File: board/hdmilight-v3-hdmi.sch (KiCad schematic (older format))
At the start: 41 parts, among them J2 HDMI_A, Q2 BSS123, Q3 BSS123, Q4 BSS123, U4 ADV7611, U6 TPD12S520, Y2 28.63636MHz

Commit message: Fixed bugs in v3.0 board:
 * Changed FPGA GPIO to 2 row with ground to make it compatible with logic analyser plug for debugging
 * Move position sensor from PB4 to PB5
 * Connect voltage regulator center pad to ground pins
 * Add SPI CS line between FPGA and MCU
 * Move HDMI hotplug LED back from board edge
 * Move HDMI ESD chip closer to connector
 * Swap serial rx/tx
 * Fix FPGA EEPROM footprint
 * Fix reset button footprint
 * Connect ADV I2C to MCU
 * Fix missing ground to hotplug power off circuit
 * Move LED power connector to back of board
 * Move standby button to front of board
 * Only use HDMI 5v for hotplug detect
 * Change LED power switching to high side to stop it grounding back through the data line
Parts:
- R60: value 1K -> 2K2
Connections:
- net GND: now also Q2.2 (S), Q4.2 (S)
- net HDMI_5V: no longer C10.1, R14.1, R15.1, R60.2, U6.1 (5V)
- new net +5V: C10.1, R14.1, R15.1, R60.2, U6.1 (5V)
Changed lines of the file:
@@
 Wire Wire Line
 	2400 1300 2400 950
-Wire Wire Line
-	2400 950  2450 950
 Connection ~ 2400 1300
 Wire Wire Line
 	2400 1300 2550 1300
-Text GLabel 2450 950  2    50   Input ~ 0
-HDMI_5V
-Wire Wire Line
-	3800 1250 3900 1250
 Wire Wire Line
 	3800 1250 3800 1400
-Text GLabel 3900 1250 2    50   Input ~ 0
-HDMI_5V
 $Comp
 L Transistor_FET:BSS123 Q3
@@
 P 5850 4050
 F 0 "R60" V 6057 4050 50  0000 C CNN
-F 1 "1K" V 5966 4050 50  0000 C CNN
+F 1 "2K2" V 5966 4050 50  0000 C CNN
 F 2 "Resistor_SMD:R_0603_1608Metric" V 5780 4050 50  0001 C CNN
 F 3 "~" H 5850 4050 50  0001 C CNN
@@
 $EndComp
 Wire Wire Line
-	6000 4050 6100 4050
+	6000 4050 6200 4050
 Wire Wire Line
 	5600 4050 5700 4050
@@
 	2200 5750 2200 5450
 Wire Wire Line
-	1850 5750 2200 5750
+	1850 5750 2050 5750
 Wire Wire Line
 	1850 5700 1850 5750
@@
 	600  4700 2800 4700
 Wire Notes Line
-	2800 4700 2800 6000
-Wire Notes Line
-	2800 6000 600  6000
-Wire Notes Line
-	600  6000 600  4700
-Text Notes 1850 5950 2    50   ~ 0
+	2800 4700 2800 6050
+Wire Notes Line
+	2800 6050 600  6050
+Wire Notes Line
+	600  6050 600  4700
+Text Notes 1850 6000 2    50   ~ 0
 Pull HPD low when powered off
 $Comp
@@
 	1    0    0    -1
 $EndComp
-Text GLabel 6100 4050 2    50   Input ~ 0
-HDMI_5V
 $Comp
 L Device:Crystal_Small Y2
@@
 	1000 4100 1100 4100
 NoConn ~ 1700 3500
+$Comp
+L power:+5V #PWR0194
+U 1 1 5E441643
+P 2400 950
+F 0 "#PWR0194" H 2400 800 50  0001 C CNN
+F 1 "+5V" H 2415 1123 50  0000 C CNN
+F 2 "" H 2400 950 50  0001 C CNN
+F 3 "" H 2400 950 50  0001 C CNN
+	1    2400 950
+	1    0    0    -1
+$EndComp
+$Comp
+L power:+5V #PWR0195
+U 1 1 5E44BA2A
+P 3800 1250
+F 0 "#PWR0195" H 3800 1100 50  0001 C CNN
+F 1 "+5V" H 3815 1423 50  0000 C CNN
+F 2 "" H 3800 1250 50  0001 C CNN
+F 3 "" H 3800 1250 50  0001 C CNN
+	1    3800 1250
+	1    0    0    -1
+$EndComp
+$Comp
+L power:+5V #PWR0196
+U 1 1 5E4559E2
+P 6200 3900
+F 0 "#PWR0196" H 6200 3750 50  0001 C CNN
+F 1 "+5V" H 6215 4073 50  0000 C CNN
+F 2 "" H 6200 3900 50  0001 C CNN
+F 3 "" H 6200 3900 50  0001 C CNN
+	1    6200 3900
+	1    0    0    -1
+$EndComp
+Wire Wire Line
+	6200 3900 6200 4050
+$Comp
+L power:GND #PWR0197
+U 1 1 5EDA9DEE
+P 2050 5800
+F 0 "#PWR0197" H 2050 5550 50  0001 C CNN
+F 1 "GND" H 2055 5627 50  0000 C CNN
+F 2 "" H 2050 5800 50  0001 C CNN
+F 3 "" H 2050 5800 50  0001 C CNN
+	1    2050 5800
+	1    0    0    -1
+$EndComp
+Wire Wire Line
+	2050 5750 2050 5800
+Connection ~ 2050 5750
+Wire Wire Line
+	2050 5750 2200 5750
 Wire Bus Line
 	9900 1900 9900 4450

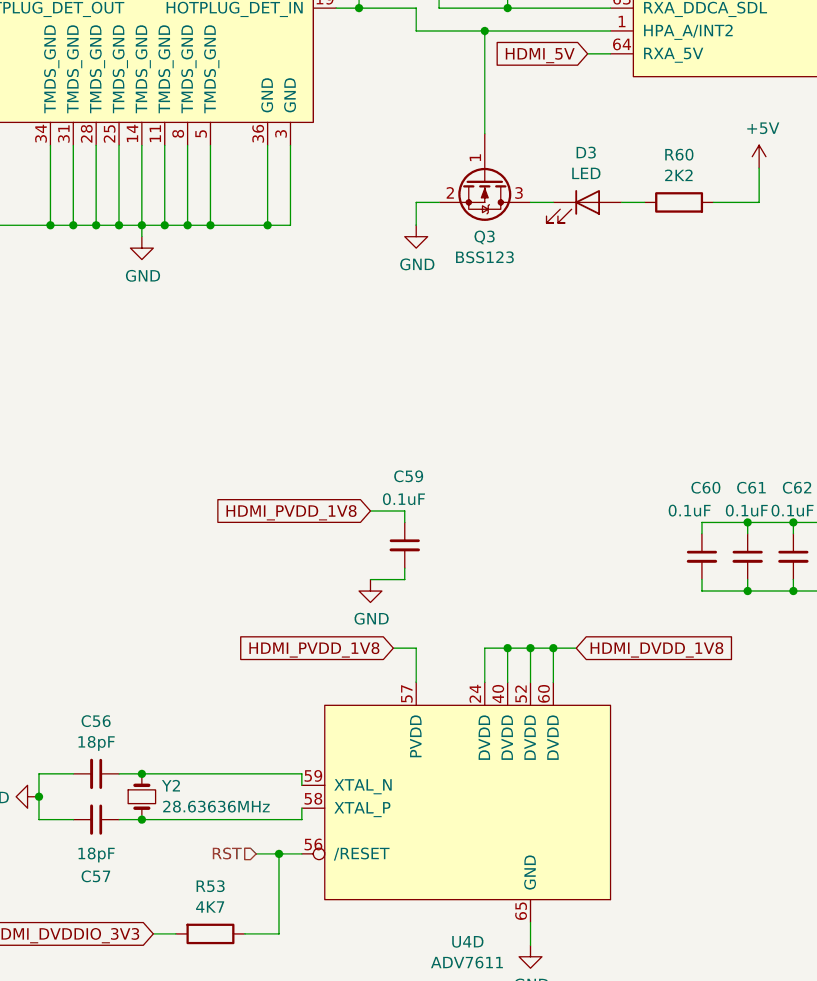
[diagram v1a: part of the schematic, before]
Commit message: Updated BOM with individual LED colours/types
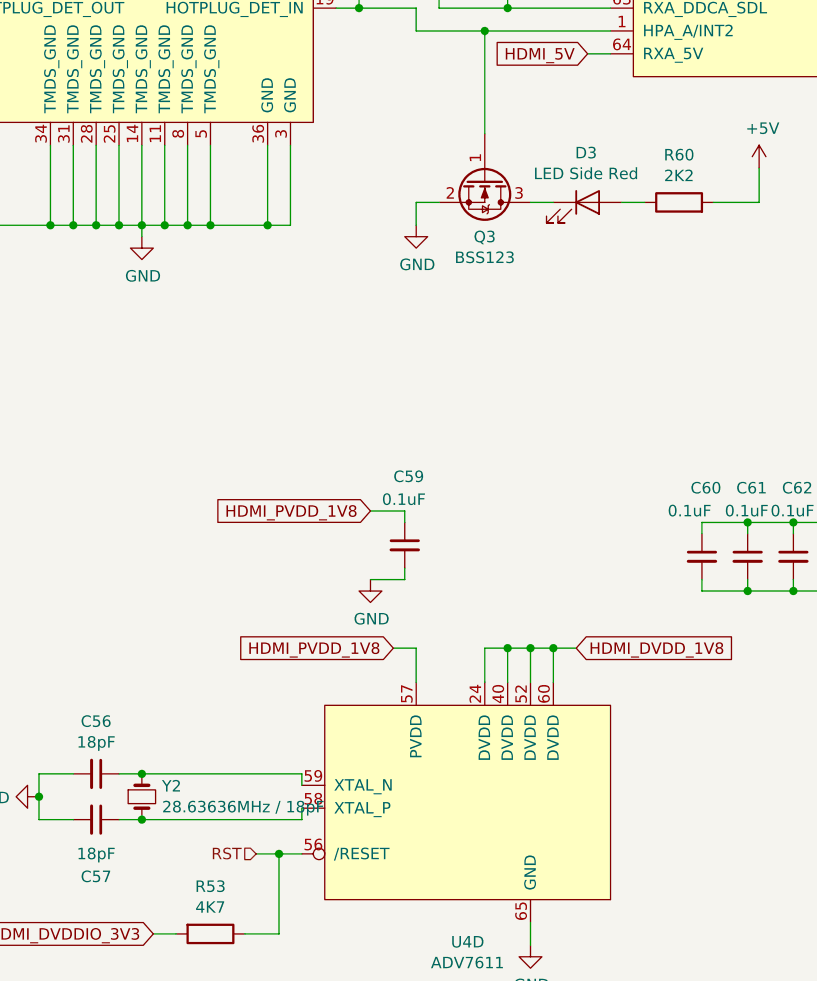
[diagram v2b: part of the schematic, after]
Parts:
- D3: value LED -> LED Side Red
- Y2: value 28.63636MHz -> 28.63636MHz / 18pF
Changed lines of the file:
@@
 P 5450 4050
 F 0 "D3" H 5443 4266 50  0000 C CNN
-F 1 "LED" H 5443 4175 50  0000 C CNN
+F 1 "LED Side Red" H 5443 4175 50  0000 C CNN
 F 2 "LED_SMD:LED_0603_1608Metric" H 5450 4050 50  0001 C CNN
 F 3 "~" H 5450 4050 50  0001 C CNN
@@
 P 3500 6650
 F 0 "Y2" V 3454 6738 50  0000 L CNN
-F 1 "28.63636MHz" V 3545 6738 50  0000 L CNN
+F 1 "28.63636MHz / 18pF" V 3545 6738 50  0000 L CNN
 F 2 "Crystal:Crystal_SMD_5032-2Pin_5.0x3.2mm" H 3500 6650 50  0001 C CNN
 F 3 "~" H 3500 6650 50  0001 C CNN
